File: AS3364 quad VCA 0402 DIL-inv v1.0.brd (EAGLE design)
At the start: 41.3 x 16.2 mm, 45 parts, among them IC1 TL072JD, IC2 TL072JD

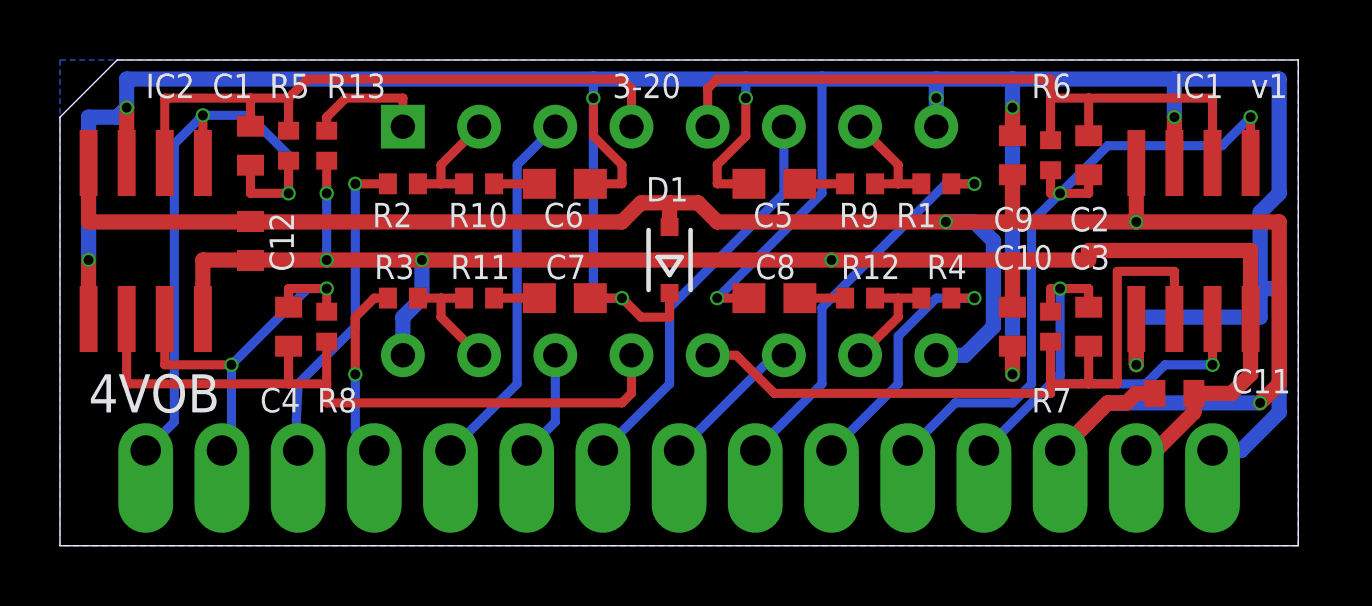
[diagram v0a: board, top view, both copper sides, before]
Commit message: Added AS3364 versions of quad VCA
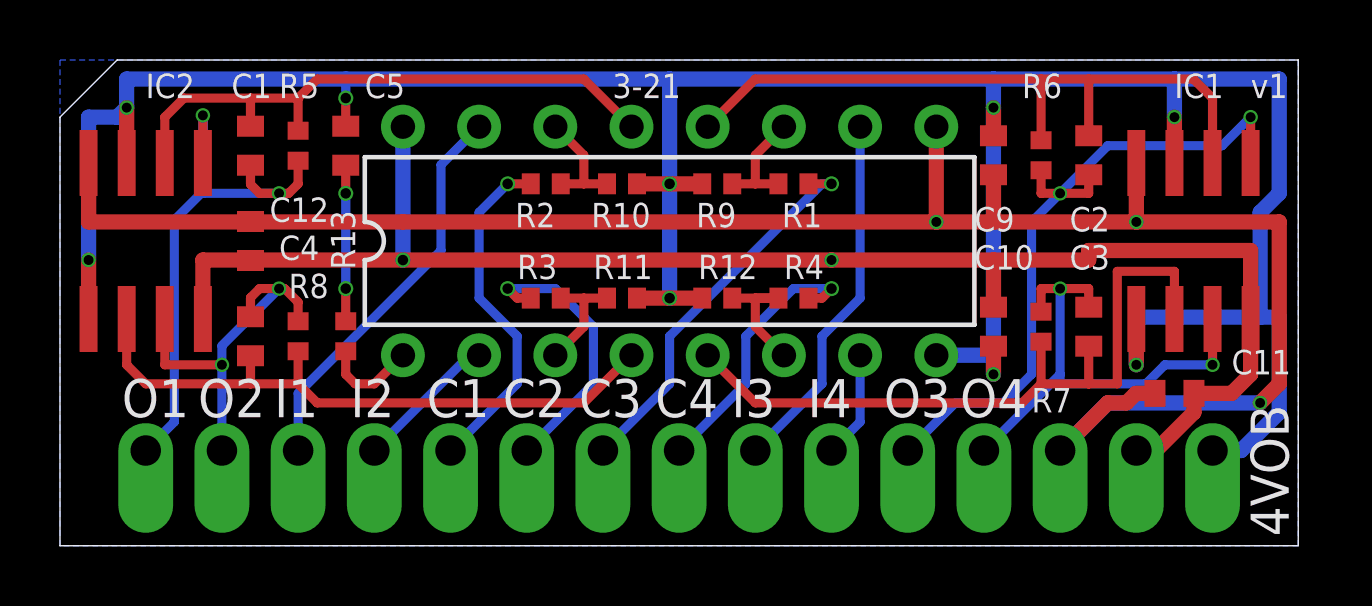
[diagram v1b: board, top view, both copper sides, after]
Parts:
- removed C6, C7, C8: 560pF, rcl:C0603
- removed D1: B5817, diode:SOD323-R
- removed DA1: V2164D, ic-coolaudio:DIP-16
- added DA2: AS3364D, joakim:DIL16J
- C1, C2, C3, C4: value 100pF -> 33pF
- C5: value 560pF -> 5nF; device rcl:C0603 -> rcl:C0402
- R1, R2, R3, R4, R5, R6, R7, R8: value 30k -> 47k
- R10, R11, R12, R9: value 500R -> 47k
- R13: value 7.5k for A -> 100R
- moved C5 14.3 mm to (9.53, 13.3), turned to 270 degrees
- moved R13 6.38 mm to (9.53, 6.99), turned to 270 degrees
- moved R12 4.76 mm to (21.9, 8.26)
- moved R9 4.76 mm to (21.9, 12.1)
- moved R10 4.76 mm to (18.7, 12.1)
- moved R11 4.76 mm to (18.7, 8.26)
- moved R1 4.76 mm to (24.4, 12.1)
- moved R2 4.76 mm to (16.2, 12.1)
- moved R3 4.76 mm to (16.2, 8.26)
- moved R4 4.76 mm to (24.4, 8.26)
- moved C4 1.31 mm to (6.35, 6.99)
- moved R8 1.00 mm to (7.94, 6.99)
- moved C10 0.64 mm to (31.1, 7.30)
- moved C9 0.64 mm to (31.1, 13.0)
- moved R6 0.32 mm to (32.7, 13.0)
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- renumbered +15V to +12V, -15V to -12V
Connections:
- removed net +15V: +12V.1, C10.2, C11.2, C12.2, DA1.16, IC1.8, IC2.8, R13.1
- removed net -15V: -12V.1, C11.1, C12.1, C9.1, D1.A, DA1.9, IC1.4, IC2.4
- removed net C1: CV1.1, DA1.3
- removed net C2: CV2.1, DA1.14
- removed net C3: CV3.1, DA1.6
- removed net C4: CV4.1, DA1.11
- removed net N$11: C7.2, R11.1
- removed net N$17: DA1.7, R1.2, R9.2
- removed net N$18: DA1.2, R10.2, R2.2
- removed net N$19: DA1.15, R11.2, R3.2
- removed net N$20: DA1.10, R12.2, R4.2
- removed net N$9: C5.2, R9.1
- new net +12V: +12V.1, C10.2, C11.2, C12.2, DA2.16, IC1.8, IC2.8
- new net -12V: -12V.1, C11.1, C12.1, C9.1, DA2.9, IC1.4, IC2.4
- new net CV1: CV1.1, R2.1
- new net CV2: CV2.1, R3.1
- new net CV2_IN: DA2.3, R11.2, R3.2
- new net CV3: CV3.1, R1.1
- new net CV4: CV4.1, R4.1
- new net N$14: C5.2, R13.1
- new net N$21: DA2.14, R10.2, R2.2
- net GND: now also DA2.8, R10.1, R11.1, R12.1, R9.1; no longer C6.1, C7.1, C8.1, D1.C, DA1.8
- net IN1: now also DA2.15; no longer R2.1
- net IN2: now also DA2.2; no longer R3.1
- net IN3: now also DA2.10; no longer R1.1
- net IN4: now also DA2.7; no longer R4.1
- net N$1: now also DA2.4; no longer DA1.13
- net N$10: now also DA2.6, R12.2, R4.2; no longer C6.2, R10.1
- net N$12: now also DA2.11, R1.2, R9.2; no longer C8.2, R12.1
- net N$2: now also DA2.1; no longer DA1.1
- net N$3: now also DA2.5; no longer DA1.12
- net N$5: now also DA2.12; no longer DA1.5
- net N$7: now also DA2.13; no longer DA1.4
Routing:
- net -15V: track 71.1 -> 0.00 mm, vias 3 -> 0
- net -12V: track 0.00 -> 65.9 mm, vias 0 -> 3
- net +15V: track 54.9 -> 0.00 mm, vias 4 -> 0
- net +12V: track 0.00 -> 52.6 mm, vias 0 -> 2
- net GND: track 119.4 -> 101.0 mm, vias 11 -> 9
- net C3: track 13.3 -> 0.00 mm
- net CV3: track 0.00 -> 13.0 mm, vias 0 -> 1
- net C1: track 12.2 -> 0.00 mm
- net CV1: track 0.00 -> 11.5 mm, vias 0 -> 1
- net CV2: track 0.00 -> 9.33 mm, vias 0 -> 1
- net CV4: track 0.00 -> 9.15 mm, vias 0 -> 1
- net N$14: track 0.00 -> 5.20 mm, vias 0 -> 2
- net IN4: track 8.57 -> 3.57 mm, vias 1 -> 0
- net C4: track 4.81 -> 0.00 mm
- net N$19: track 3.97 -> 0.00 mm
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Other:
- board text added: "+12v"
- board text added: "-12v"
- board text added: "3-21"
- board text added: "NB: Max 26V diff"
- board text added: "Quad lin inv VCA"
- board text removed: "+15v"
- board text removed: "-15v"
- board text removed: "3-20"
- board text removed: "Mount socket on this side!"
- board text removed: "Quad exp VCA"

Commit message: Turned pads to make it possible to solder angled legs
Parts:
- moved +12V 1.90 mm to (35.9, 1.27), turned to 180 degrees
- moved -12V 1.90 mm to (33.3, 1.27), turned to 180 degrees
- moved CV1 1.90 mm to (13.0, 1.27), turned to 180 degrees
- moved CV2 1.90 mm to (15.6, 1.27), turned to 180 degrees
- moved CV3 1.90 mm to (18.1, 1.27), turned to 180 degrees
- moved CV4 1.90 mm to (20.6, 1.27), turned to 180 degrees
- moved GND 1.90 mm to (38.4, 1.27), turned to 180 degrees
- moved IN1 1.90 mm to (7.94, 1.27), turned to 180 degrees
- moved IN2 1.90 mm to (10.5, 1.27), turned to 180 degrees
- moved IN3 1.90 mm to (23.2, 1.27), turned to 180 degrees
- moved IN4 1.90 mm to (25.7, 1.27), turned to 180 degrees
- moved OUT1 1.90 mm to (2.86, 1.27), turned to 180 degrees
- moved OUT2 1.90 mm to (5.40, 1.27), turned to 180 degrees
- moved OUT3 1.90 mm to (28.3, 1.27), turned to 180 degrees
- moved OUT4 1.90 mm to (30.8, 1.27), turned to 180 degrees
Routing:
- net -12V: track 65.9 -> 69.8 mm
- net OUT4: track 16.6 -> 18.5 mm
- net OUT3: track 23.5 -> 25.4 mm
- net OUT1: track 21.9 -> 23.8 mm
- net IN1: track 13.3 -> 15.2 mm
- net CV3: track 13.0 -> 14.9 mm
- net IN2: track 4.81 -> 6.71 mm
- net IN4: track 3.57 -> 5.47 mm
- net IN3: track 12.2 -> 14.1 mm
- net CV4: track 9.15 -> 11.1 mm
- net CV2: track 9.33 -> 11.2 mm
- net CV1: track 11.5 -> 13.4 mm
- net OUT2: track 12.8 -> 14.7 mm
- net +12V: track 52.6 -> 54.1 mm
- net GND: track 101.0 -> 102.3 mm
